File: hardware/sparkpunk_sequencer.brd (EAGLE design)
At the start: 165.1 x 88.6 mm, 139 parts, among them IC1 7555, IC3 LM358, IC4 LM358, IC5 CD4013B, IC6 CD4017, Q100 2N3904, Q1000 2N3904, Q200 2N3904, Q300 2N3904, Q400 2N3904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

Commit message: PCB updates after review
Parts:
- removed R12, R9: 10k, SparkFun-Resistors:AXIAL-0.3EZ
- added JP3: TEMPO_CV, SparkFun-Connectors:1X01NS
- added LOGO4: SFE_LOGO_NAME_FLAME.4_INCH, SparkFun-Aesthetics:SFE_LOGO_NAME_FLAME_.4
- added R20, R21, R22, R25: 10k, SparkFun-Resistors:AXIAL-0.3EZ
- added R23, R24: 10k*, SparkFun-Resistors:AXIAL-0.3EZ
- added SJ6**: NON-INV-N.O., SparkFun-Passives:SJ_2S-PTH
- JP10: value TRANSPOSE -> TNG-GND
- R10: value 10k -> 10k*
- S3: value SWITCH-MOMENTARY-LEDEZ -> Play Button
- SJ1: value RUN -> RUN-N.C.
- SJ2: value STOP -> STOP-N.C.
- SJ3: value CLK -> CLK-N.C.
- SJ4: value BTN -> BTN-N.C.
- SJ5: value ONE-SHOT -> ONE-SHOT-N.O.
- moved LOGO1 35.9 mm to (102.9, 27.9)
- moved JP10 16.5 mm to (1.27, 80.0)
- moved JP7 16.5 mm to (1.27, 77.5)
- moved LED1 7.24 mm to (24.8, 51.4)
- moved R15 2.54 mm to (48.3, 72.4)
- moved R16 2.54 mm to (45.7, 72.4)
- moved BAT1 1.27 mm to (48.3, 56.5)
- moved R10 1.27 mm to (6.35, 72.4)
- moved R8 1.27 mm to (6.35, 74.9)
- turned R7 to 180 degrees
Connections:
- removed net CVSUM: IC3.3, R10.P$1, R12.P$1
- new net N$64: IC3.6, R20.P$1, R25.P$2
- new net N$65: IC3.5, R21.P$2, R22.P$2
- new net VREF: IC3.3, R23.P$1, R24.P$2, SJ6**.2
- net GND: now also R24.P$1, R25.P$1; no longer R9.P$1
- net N$12: now also R7.P$1; no longer R7.P$2
- net N$15: now also R10.P$1; no longer R9.P$2
- net N$16: now also R22.P$1; no longer R12.P$2
- net N$17: now also R20.P$2; no longer IC3.6
- net N$18: now also R21.P$1; no longer IC3.5
- net N$7: now also JP3.1
- net POTSUM: now also SJ6**.1
- net VCC: now also R23.P$2, R7.P$2; no longer R7.P$1
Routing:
- net N$65: track 0.00 -> 24.2 mm, vias 0 -> 2
- net VREF: track 0.00 -> 24.2 mm, vias 0 -> 1
- net GND: track 574.2 -> 597.1 mm
- net N$64: track 0.00 -> 20.2 mm
- net POTSUM: track 227.3 -> 243.6 mm, vias 2 -> 3
- net N$18: track 111.6 -> 119.0 mm, vias 3 -> 4
- net VCC: track 334.7 -> 341.9 mm
- net N$13: track 16.1 -> 9.04 mm
- net CVSUM: track 5.97 -> 0.00 mm
- net CLK-IN: track 77.7 -> 81.3 mm
- net N$17: track 37.9 -> 34.6 mm, vias 2 -> 3
- net N$22: track 8.29 -> 11.6 mm
- net N$7: track 9.11 -> 12.4 mm
- net N$23: track 3.43 -> 6.50 mm
- net N$16: track 13.2 -> 15.8 mm
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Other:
- board text added: "+"
- board text added: "CLK CV IN"
- board text added: "CV OUT"
- board text added: "GATE OUT"
- board text added: "SJ6"
- board text added: "TRANSP-IN"
- board text removed: "CV"
- board text removed: "GATE"
- board text removed: "TRANSP"

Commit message: Small updates after creating BOM
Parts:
- C1: value .1 -> .1uf
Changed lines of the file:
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@@
 <attribute name="PROD_ID" value="RES-09435" x="22.86" y="29.21" size="1.778" layer="27" rot="R180" display="off"/>
 </element>
-<element name="C1" library="SparkFun-Capacitors" package="CAP-PTH-SMALL-KIT" value=".1" x="22.86" y="35.56">
+<element name="C1" library="SparkFun-Capacitors" package="CAP-PTH-SMALL-KIT" value=".1uf" x="22.86" y="35.56">
 <attribute name="PROD_ID" value="CAP-08370" x="22.86" y="35.56" size="1.778" layer="27" font="vector" ratio="15" display="off"/>
 </element>

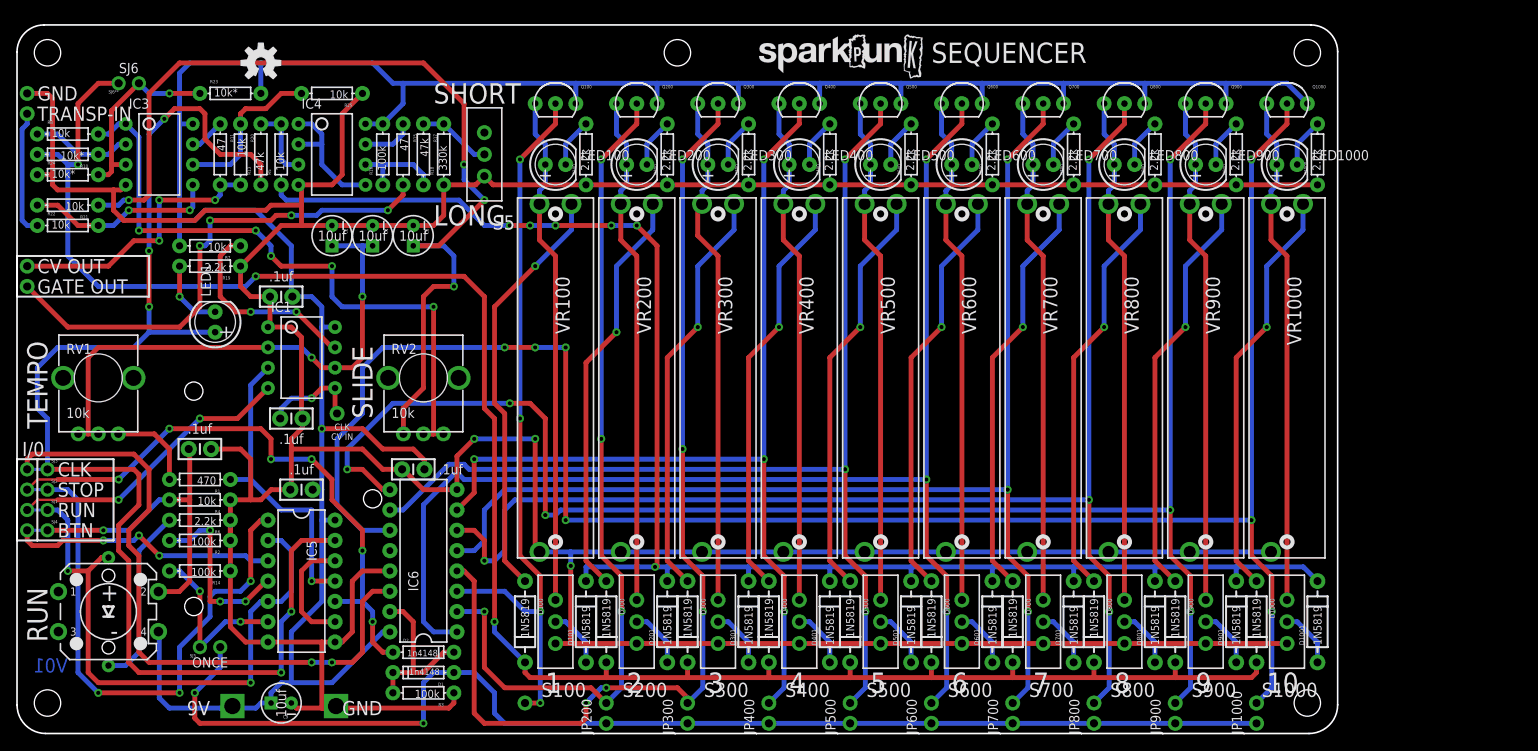
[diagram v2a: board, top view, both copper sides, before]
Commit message: Ready for second prototype
Many changes based on prototype evaluation.
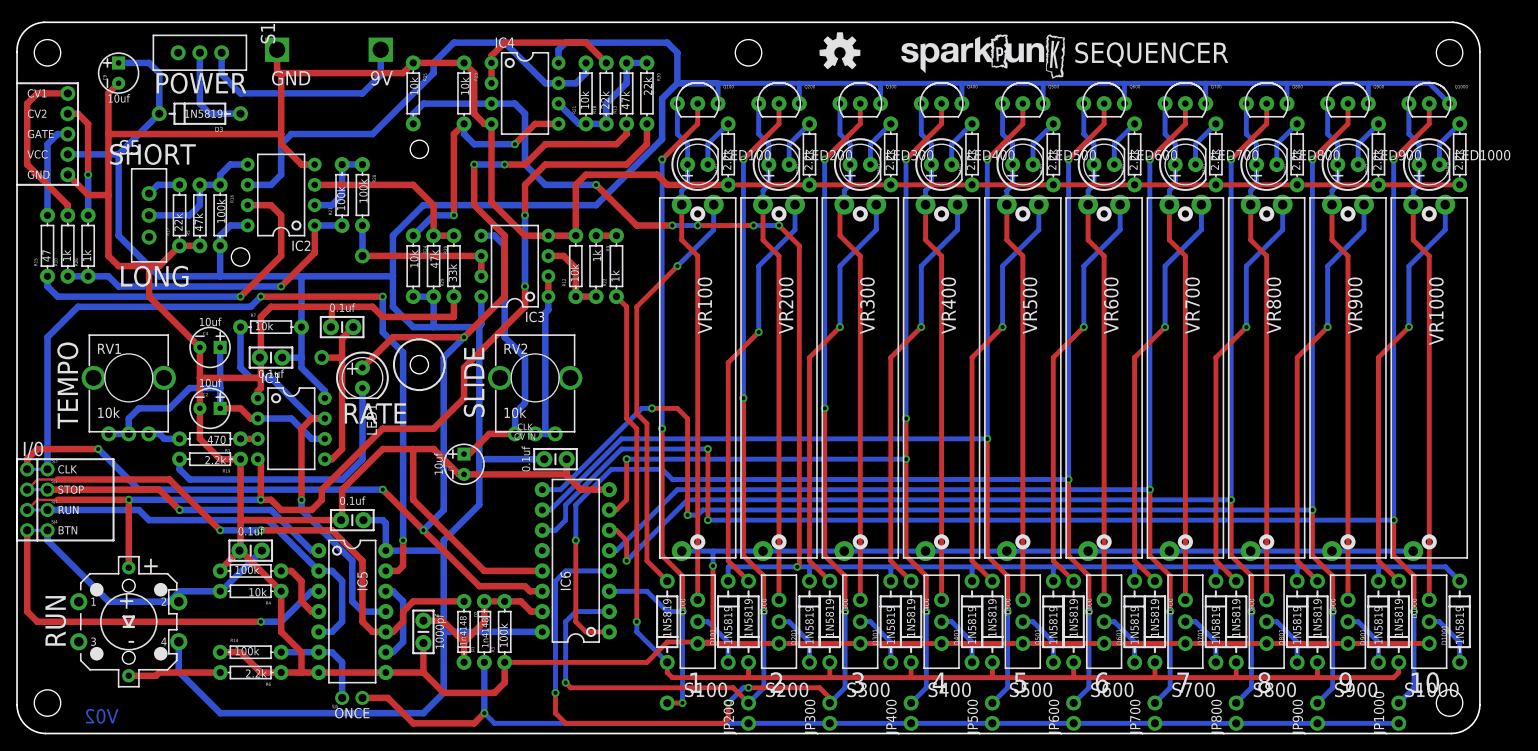
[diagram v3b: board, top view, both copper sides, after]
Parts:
- removed JP10: TNG-GND, SparkFun-Connectors:1X01NS
- removed R11: 47, SparkFun-Resistors:AXIAL-0.3EZ
- removed R8: 10k, SparkFun-Resistors:AXIAL-0.3EZ
- removed SJ6**: NON-INV-N.O., SparkFun-Passives:SJ_2S-PTH
- added C10: 1nf, SparkFun-Capacitors:CAP-PTH-SMALL-KIT
- added D3: 1N5819, SparkFun-DiscreteSemi:DIODE-1N4001-KIT
- added IC2: LM358, SparkFun-AnalogIC:DIP08-KIT
- added JP4: CV2, SparkFun-Connectors:1X01NS
- added JP5: CV, SparkFun-Connectors:1X01NS
- added JP6: VCC, SparkFun-Connectors:1X01NS
- added R12: 10k, SparkFun-Resistors:AXIAL-0.3EZ
- added R26, R9: 1k, SparkFun-Resistors:AXIAL-0.3EZ
- added R27, R28: 100k, SparkFun-Resistors:AXIAL-0.3EZ
- added R29: 33k, SparkFun-Resistors:AXIAL-0.3EZ
- added R30: 22k, SparkFun-Resistors:AXIAL-0.3EZ
- added S1: SPDT, SparkFun-Electromechanical:SWITCH-SPDT_KIT
- BAT1: device SparkFun-Connectors:BC9VPC -> SparkFun-Connectors:BC9VPC_KIT
- JP2: value CV -> CV1
- JP7: value TRANSPOSE -> GND
- R10: value 10k* -> 1k
- R17: value 47k -> 22k
- R18: value 330k -> 22k
- R20, R5: value 10k -> 47k
- R22: value 10k -> 1k
- R23, R24: value 10k* -> 10k
- moved C9 81.3 mm to (12.7, 82.5), turned to 90 degrees
- moved LOGO2 72.4 mm to (102.9, 85.1)
- moved R22 68.8 mm to (74.9, 58.4), turned to 90 degrees
- moved R21 66.3 mm to (71.1, 80.0), turned to 90 degrees
- moved IC3 46.6 mm to (62.2, 58.4), turned to 90 degrees
- moved R13 46.4 mm to (76.2, 80.0)
- moved R15 45.9 mm to (3.81, 61.0), turned to 90 degrees
- moved R24 44.7 mm to (49.5, 58.4), turned to 270 degrees
- moved S5 42.6 mm to (16.5, 64.8), turned to 0 degrees
- moved BAT1 34.1 mm to (24.1, 32.4), turned to 90 degrees
- moved R17 31.4 mm to (20.3, 64.8), turned to 90 degrees
- moved C3 29.3 mm to (55.9, 33.7), turned to 90 degrees
- moved R23 29.2 mm to (55.9, 80.0), turned to 270 degrees
- moved R20 27.9 mm to (52.1, 58.4)
- moved C2 26.4 mm to (24.1, 40.6), turned to 0 degrees
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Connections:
- removed net N$12: IC1.7, R7.P$1
- removed net N$20 (its old number): IC4.1, IC4.2, IC4.5
- removed net VREF: IC3.3, R23.P$1, R24.P$2, SJ6**.2
- new net 555OUT: IC1.3, R1.P$1
- new net N$66: IC2.1, R10.P$1, R26.P$1, R27.P$1
- new net N$67: JP4.1, R26.P$2
- new net N$68: JP2.1, R10.P$2
- new net N$69: IC2.6, IC4.7, R21.P$2
- new net N$70: IC4.5, R23.P$2, R24.P$1
- new net N$71: D3.A, S1.2
- new net VBATT: BAT1.V+, S1.1
- net CLK-IN: now also LED1.A, R13.P$1
- net CLK-OUT: no longer LED1.A, R13.P$1
- net GATESUM: now also IC4.3, R25.P$2; no longer R5.P$1
- net GND: now also C10.2, IC2.4, JP7.1, R12.P$2, R17.P$1, R23.P$1, R29.P$1, R5.P$1; no longer JP10.1, R18.P$1, R24.P$1, S5.1
- net N$11: now also IC4.1, IC4.2, R18.P$2; no longer IC4.3, R13.P$2, R5.P$2
- net N$14: now also C10.1
- net N$15: now also IC3.3, R12.P$1, R9.P$2; no longer IC3.2, R10.P$1, R8.P$1
- net N$16: now also R22.P$2, R9.P$1; no longer JP7.1, R22.P$1
- net N$17: now also IC2.2, R27.P$2, R28.P$1; no longer JP2.1, R11.P$2, R20.P$2
- net N$18: now also IC3.5; no longer R21.P$1
- net N$19: now also IC2.3, R20.P$1, R29.P$2; no longer IC3.7, R11.P$1
- net N$22: now also IC2.5, R5.P$2, S5.2; no longer IC4.6, R17.P$2
- net N$23: now also IC2.7; no longer IC4.7
- net N$25: now also R17.P$2, S5.1; no longer R17.P$1, R18.P$2, S5.2
- net N$6: now also IC3.2; no longer R8.P$2
- net N$64: now also IC4.6, R13.P$2, R18.P$1, R21.P$1, R30.P$1; no longer IC3.6, R20.P$1, R25.P$2
- net N$65: now also IC3.6, IC3.7, JP5.1, R28.P$2; no longer IC3.5, R21.P$2, R22.P$2
- net POTSUM: now also R22.P$1; no longer R10.P$2, SJ6**.1
- net PRECLK: now also IC1.7, R7.P$1; no longer IC1.3, R1.P$1
- net RUN-IN: now also R30.P$2, S3.A
- net RUN-OUT: no longer S3.A
- net VCC: now also D3.C, IC2.8, JP6.1, R20.P$2, R24.P$2; no longer BAT1.V+, R23.P$2
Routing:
- net GND: track 597.1 -> 713.7 mm, vias 3 -> 1
- net VCC: track 341.9 -> 439.5 mm, vias 1 -> 0
- net RUN-IN: track 36.4 -> 125.6 mm, vias 2 -> 4
- net POTSUM: track 243.6 -> 158.1 mm, vias 3 -> 1
- net N$18: track 119.0 -> 36.0 mm, vias 4 -> 0
- net CLK-IN: track 81.3 -> 161.2 mm, vias 2 -> 6
- net CLK-OUT: track 162.7 -> 97.7 mm, vias 5 -> 3
- net N$6: track 81.4 -> 23.6 mm, vias 5 -> 0
- net N$69: track 0.00 -> 56.5 mm
- net N$20: track 63.2 -> 12.0 mm, vias 4 -> 0
- net N$66: track 0.00 -> 40.0 mm, vias 0 -> 1
- net STEP10: track 238.8 -> 199.3 mm, vias 7 -> 5
- net N$23: track 6.50 -> 42.9 mm, vias 0 -> 1
- net N$70: track 0.00 -> 32.7 mm, vias 0 -> 2
- net STOP-OUT: track 68.2 -> 37.1 mm, vias 3 -> 1
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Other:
- board size 165.1 x 88.6 mm -> 182.9 x 88.9 mm
- board text added: "0.1uf"
- board text added: "1000pf"
- board text added: "CV1"
- board text added: "CV2"
- board text added: "GATE"
- board text added: "POWER"
- board text added: "RATE"
- board text added: "V02"
- board text added: "VCC"
- board text removed: ".1uf"
- board text removed: "CV OUT"
- board text removed: "GATE OUT"
- board text removed: "SJ6"
- board text removed: "TRANSP-IN"
- board text removed: "V01"

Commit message: Ready for red review
Incorporating all changes from second round of protos, builder feedback,
etc.
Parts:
- added C11: .1uf, SparkFun-Capacitors:CAP-PTH-SMALL-KIT
- C9: value 10uf -> 1000uf/25V; device SparkFun-Capacitors:CPOL-RADIAL-10UF-25V-KIT -> SparkFun-Capacitors:CPOL-RADIAL-1000UF-25V-KIT
- moved C9 25.4 mm to (38.1, 82.5), flipped to the bottom, turned to 0 degrees
- moved BAT1 11.4 mm to (24.1, 21.0)
- moved JP5 2.54 mm to (45.7, 59.7)
- moved R20 2.54 mm to (52.1, 61.0)
- moved R24 2.54 mm to (49.5, 61.0)
- moved R29 2.54 mm to (54.6, 61.0)
- moved R1 1.42 mm to (22.9, 36.2)
- moved R19 1.42 mm to (22.9, 33.7)
- moved C8 1.42 mm to (41.9, 51.4), turned to 90 degrees
- moved D3 1.27 mm to (21.6, 77.5)
- moved C3 1.27 mm to (57.1, 33.7)
- moved SJ5 0.64 mm to (41.9, 3.81)
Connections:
- net GND: now also C9.-; no longer C9.2
- net N$63: now also C11.2
- net VCC: now also C11.1, C9.+; no longer C9.1
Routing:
- net VCC: track 439.5 -> 465.6 mm
- net GND: track 713.7 -> 694.2 mm
- net N$63: track 12.6 -> 17.5 mm
- net VBATT: track 27.7 -> 30.8 mm
- net N$70: track 32.7 -> 30.2 mm
- net N$19: track 22.3 -> 19.7 mm
- net BTN-OUT: track 36.3 -> 33.9 mm
- net N$69: track 56.5 -> 54.3 mm
- net 555OUT: track 2.16 -> 3.69 mm
- net N$71: track 12.0 -> 10.7 mm
- net N$5: track 4.11 -> 3.10 mm
- net N$7: track 21.0 -> 20.2 mm
- net N$65: track 21.2 -> 20.5 mm
- net N$13: track 34.6 -> 35.2 mm
- net PRECLK: track 50.6 -> 50.5 mm, vias 1 -> 2
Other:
- board text added: "1000uf"
- board text added: "OFF"
- board text added: "ON"
- board text added: "RAW CV OUT"
- board text added: "SEQ. RESET"
- board text added: "STEP OUT"
- board text added: "TEMPO CV IN"
- board text added: "V10"
- board text removed: "V02"
